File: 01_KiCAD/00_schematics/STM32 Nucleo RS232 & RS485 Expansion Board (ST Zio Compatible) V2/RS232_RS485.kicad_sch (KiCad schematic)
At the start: 21 parts, among them J1 1190299, J2 HEADER 3POS 2.54mm, J3 CONN D-SUB PLUG 9POS TH, J4 HEADER 3POS 2.54mm, U1 THVD4431RHAR

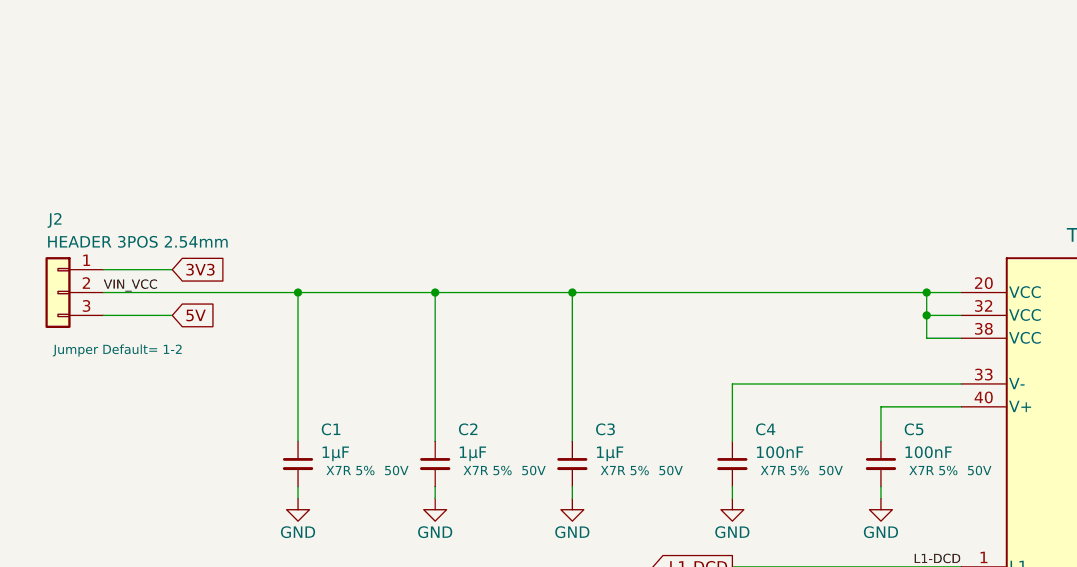
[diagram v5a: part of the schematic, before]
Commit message: Added Dual Voltage Input
Added Dual Voltage Auto Select Input drawings. Added new hierarchical sheet with new pagenumber one. All other pages have been moved up by 1.
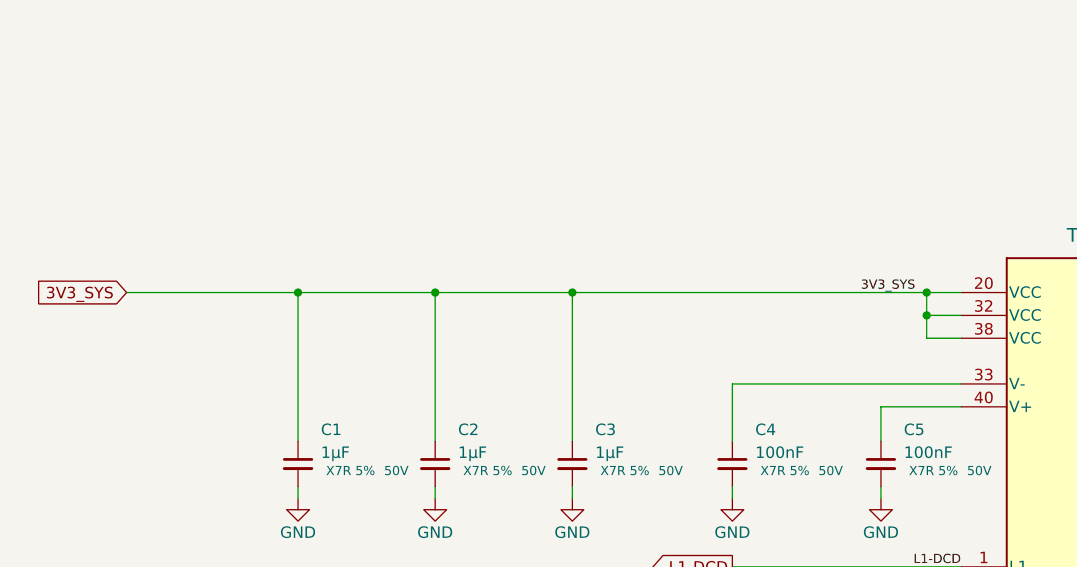
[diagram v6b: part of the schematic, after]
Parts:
- removed J2: HEADER 3POS 2.54mm, symbol Connector_Generic:Conn_01x03
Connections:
- net VIN_VCC renamed 3V3_SYS

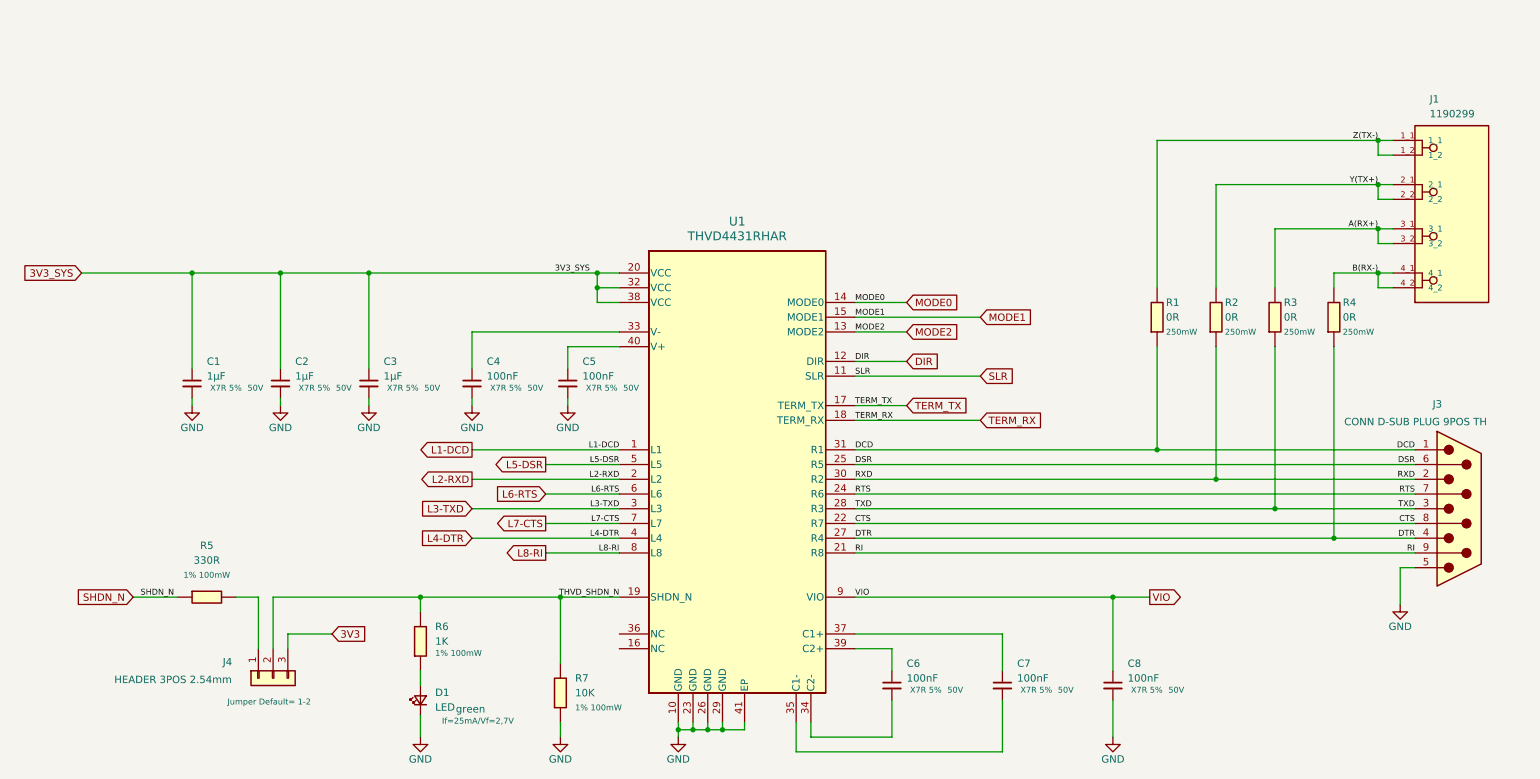
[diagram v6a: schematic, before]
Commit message: Added components and change device
Added dual Schmidt trigger input SN74LVC2G14DBV for LED Rx and Tx control.
Changed sn74hcs245 for alternate part sn74lvc245a for larger footprint and better availability with LCSC.
Difference is sn74lvc245a has no Schmidt-trigger inputs but instead just normal inputs. Fot details see dataseet. Both devices use exact same pin number and configuration except sn74lvc245a has no thermal pad or exposed pad like the sn74hcs245 has.
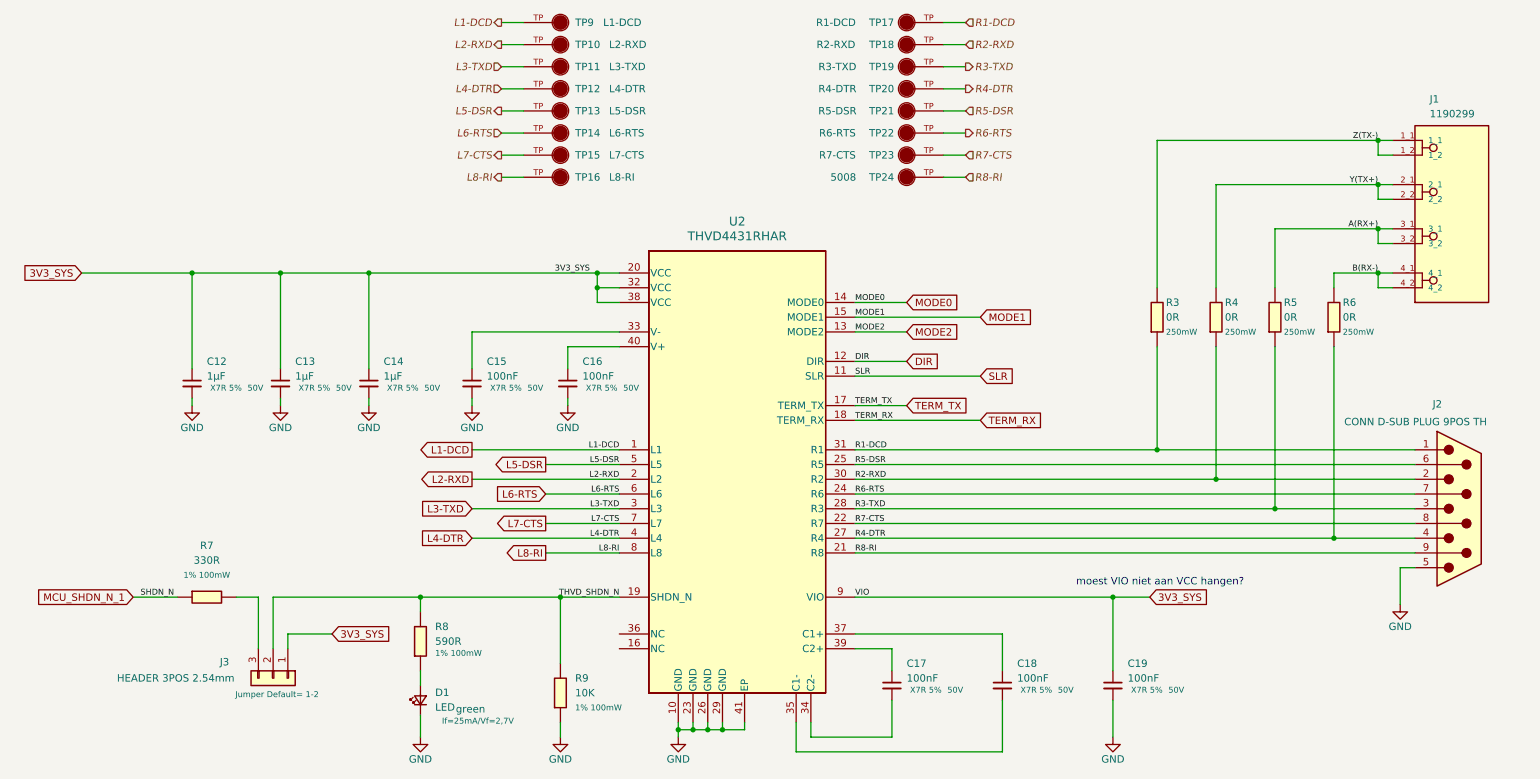
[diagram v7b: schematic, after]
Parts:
- added TP10: L2-RXD, 5009:KEYSTONE_5009, symbol 5009_Yellow:5009
- added TP11: L3-TXD, 5009:KEYSTONE_5009, symbol 5009_Yellow:5009
- added TP12: L4-DTR, 5009:KEYSTONE_5009, symbol 5009_Yellow:5009
- added TP13: L5-DSR, 5009:KEYSTONE_5009, symbol 5009_Yellow:5009
- added TP14: L6-RTS, 5009:KEYSTONE_5009, symbol 5009_Yellow:5009
- added TP15: L7-CTS, 5009:KEYSTONE_5009, symbol 5009_Yellow:5009
- added TP16: L8-RI, 5009:KEYSTONE_5009, symbol 5009_Yellow:5009
- added TP17: R1-DCD, 5008:KEYSTONE_5008, symbol 5008_Orange:5008
- added TP18: R2-RXD, 5008:KEYSTONE_5008, symbol 5008_Orange:5008
- added TP19: R3-TXD, 5008:KEYSTONE_5008, symbol 5008_Orange:5008
- added TP20: R4-DTR, 5008:KEYSTONE_5008, symbol 5008_Orange:5008
- added TP21: R5-DSR, 5008:KEYSTONE_5008, symbol 5008_Orange:5008
- added TP22: R6-RTS, 5008:KEYSTONE_5008, symbol 5008_Orange:5008
- added TP23: R7-CTS, 5008:KEYSTONE_5008, symbol 5008_Orange:5008
- added TP24: 5008, 5008:KEYSTONE_5008, symbol 5008_Orange:5008
- added TP9: L1-DCD, 5009:KEYSTONE_5009, symbol 5009_Yellow:5009
- R8: renamed from R6; value 1K -> 590R
- renumbered C1 to C12, C2 to C13, C3 to C14, C4 to C15, C5 to C16, C6 to C17, C7 to C18, C8 to C19, J3 to J2, J4 to J3, R1 to R3, R2 to R4, R3 to R5, R4 to R6, R5 to R7, R7 to R9, U1 to U2
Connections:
- net 3V3 is gone; now on an unnamed net: J3.3 (Pin_3)
- net VIO is gone; now on net 3V3_SYS: C19.1, U2.9 (VIO)
- net 3V3_SYS: now also J3.1 (Pin_1)
- net L1-DCD: now also TP9.TP
- net L2-RXD: now also TP10.TP
- net L3-TXD: now also TP11.TP
- net L4-DTR: now also TP12.TP
- net L5-DSR: now also TP13.TP
- net L6-RTS: now also TP14.TP
- net L7-CTS: now also TP15.TP
- net L8-RI: now also TP16.TP
- net at R7.1: no longer J3.1 (Pin_1)
- net CTS renamed R7-CTS
- net R7-CTS: now also TP23.TP
- net DCD renamed R1-DCD
- net R1-DCD: now also TP17.TP
- net DSR renamed R5-DSR
- net R5-DSR: now also TP21.TP
- net DTR renamed R4-DTR
- net R4-DTR: now also TP20.TP
- net RI renamed R8-RI
- net R8-RI: now also TP24.TP
- net RTS renamed R6-RTS
- net R6-RTS: now also TP22.TP
- net RXD renamed R2-RXD
- net R2-RXD: now also TP18.TP
- net SHDN_N renamed MCU_SHDN_N_1
- net TXD renamed R3-TXD
- net R3-TXD: now also TP19.TP
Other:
- note added: "moest VIO niet aan VCC hangen?"
- moved on the sheet: J3

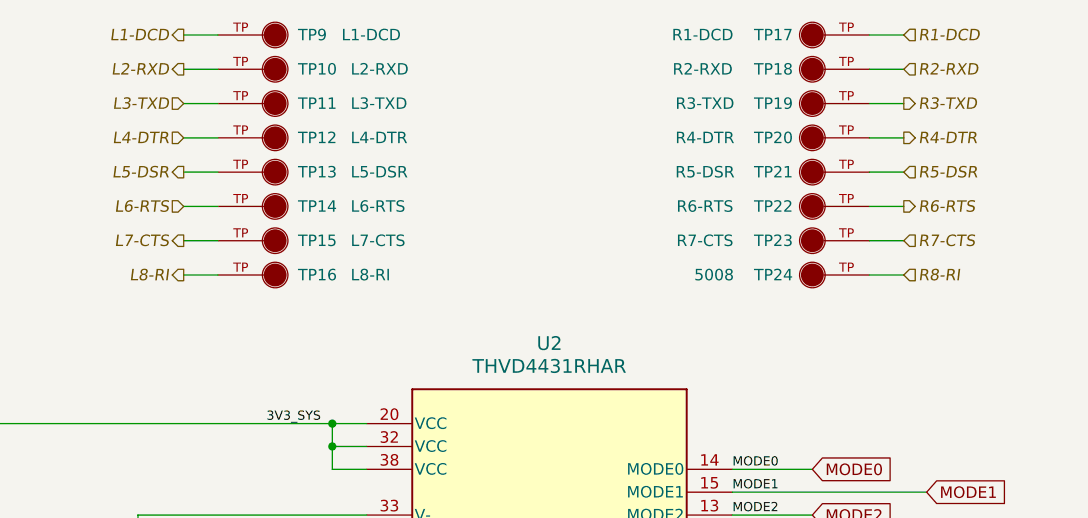
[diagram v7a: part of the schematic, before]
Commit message: Finisching touches to schematics
Finalizing the schematics and double-check all connections throughout the different sheets.
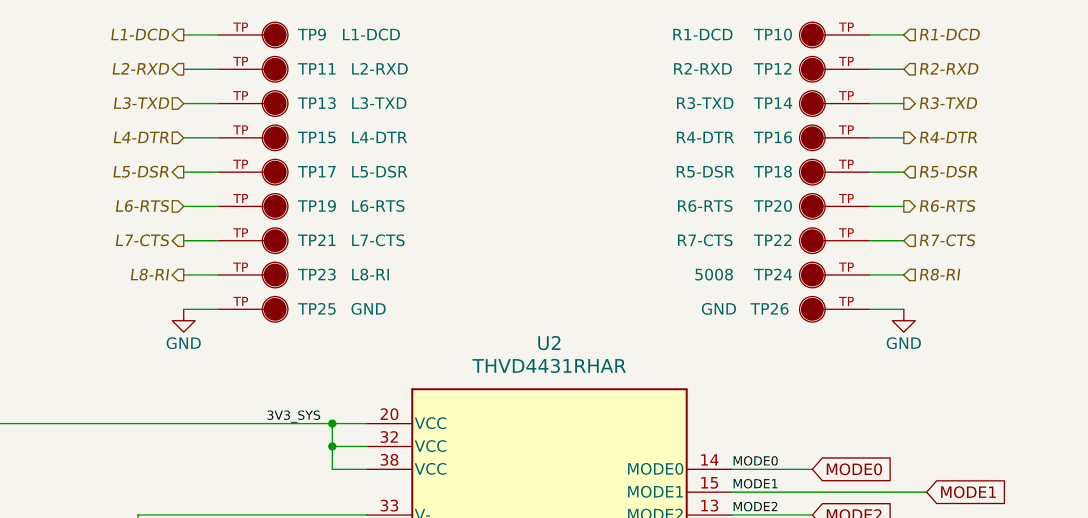
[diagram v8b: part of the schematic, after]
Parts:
- added TP25, TP26: GND, 5006:KEYSTONE_5006, symbol 5006_Black:5006
- renumbered TP17 to TP10, TP10 to TP11, TP18 to TP12, TP11 to TP13, TP19 to TP14, TP12 to TP15, TP20 to TP16, TP13 to TP17, TP21 to TP18, TP14 to TP19, TP22 to TP20, TP15 to TP21, TP23 to TP22, TP16 to TP23
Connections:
- net GND: now also TP25.TP, TP26.TP
